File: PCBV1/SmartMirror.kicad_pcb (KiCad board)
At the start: 4 copper layers, 120 x 70 mm, 194 parts, among them J1 208658-1051, J2 502570-0893, J3 10118194-0001LF, J4 PJ-102AH, SW1 SW_DIP_x05, SW2 SW_DIP_x02, U1 MCIMX6Y2CVM08AB, U10 AP62301WU-7, U11 AP62301WU-7, U12 AP62301WU-7, U13 CP2102N-A01-GQFN28, U2 MT41K128M16JT-125_K, U3 CM1624-08DE, U4 TPD3E001DRLR, U5 MCP112T-315E_LB, U6 WF200D, U7 TFP410PAP, U8 S34ML01G200BHI000, U9 MCP112T-315E_LB, Y1 ECS-384-10-33B-CKY-TR, Y2 ECS.32712.512, Y3 ECS2401823BJTM

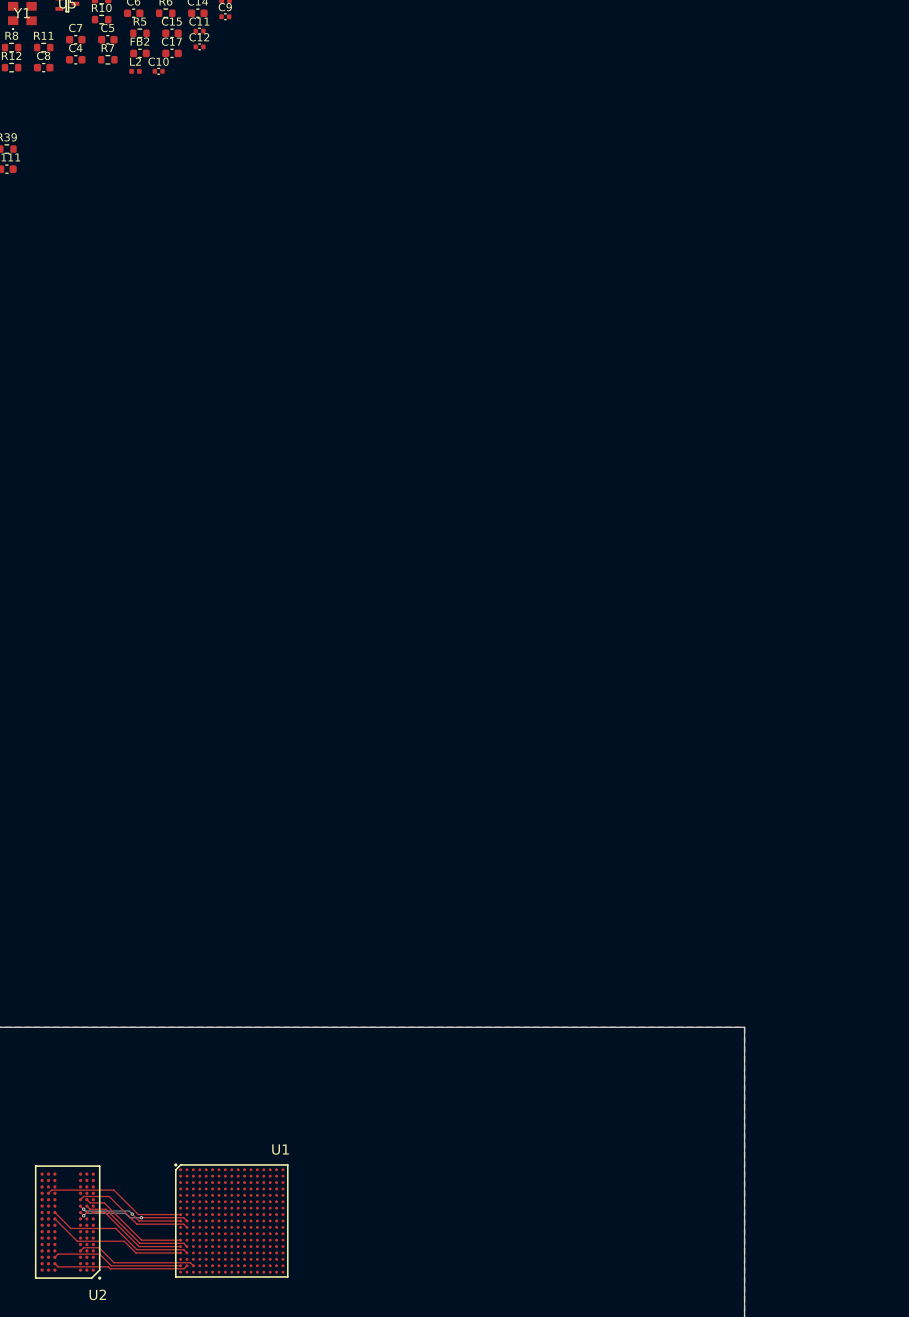
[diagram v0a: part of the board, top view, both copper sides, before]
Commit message: Added JTAG, USB OTG, USB Host, and Ethernet.
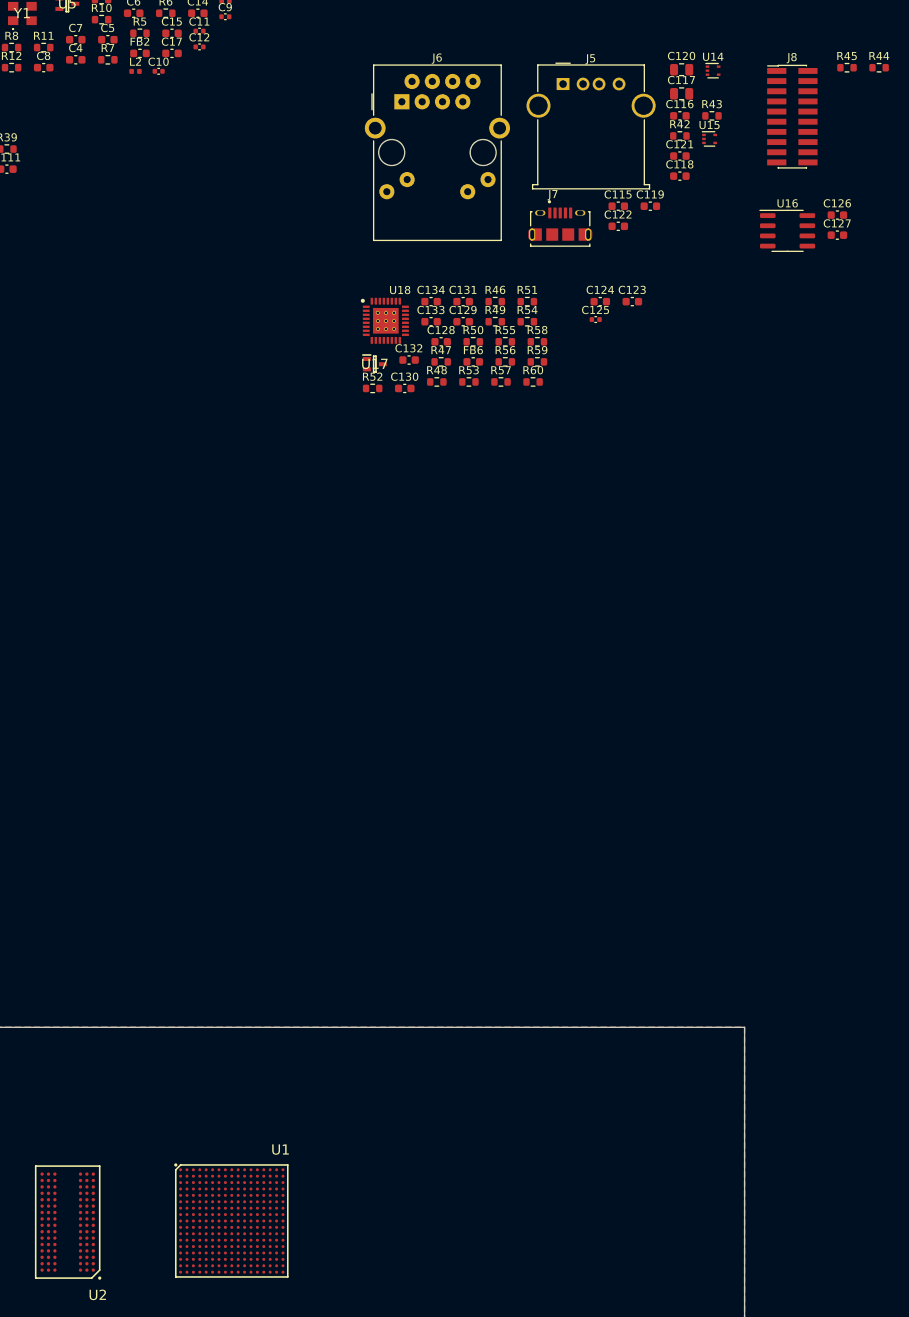
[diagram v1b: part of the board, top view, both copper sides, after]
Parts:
- added C115: 100n, Capacitor_SMD:C_0603_1608Metric, F.Cu at (199.2, -32.6)
- added C116: 100n, Capacitor_SMD:C_0603_1608Metric, F.Cu at (206.9, -43.9)
- added C117: 47u, Capacitor_SMD:C_0805_2012Metric, F.Cu at (207.1, -46.7)
- added C118: 100n, Capacitor_SMD:C_0603_1608Metric, F.Cu at (206.9, -36.4)
- added C119: 100n, Capacitor_SMD:C_0603_1608Metric, F.Cu at (203.2, -32.6)
- added C120: 47u, Capacitor_SMD:C_0805_2012Metric, F.Cu at (207.1, -49.7)
- added C121: 100n, Capacitor_SMD:C_0603_1608Metric, F.Cu at (206.9, -38.9)
- added C122: 100n, Capacitor_SMD:C_0603_1608Metric, F.Cu at (199.2, -30.1)
- added C123: 1u, Capacitor_SMD:C_0603_1608Metric, F.Cu at (201.0, -20.7)
- added C124: 1u, Capacitor_SMD:C_0603_1608Metric, F.Cu at (197.0, -20.7)
- added C125: 10u, Capacitor_SMD:C_0402_1005Metric, F.Cu at (196.4, -18.5)
- added C126: 100n, Capacitor_SMD:C_0603_1608Metric, F.Cu at (226.6, -31.5)
- added C127: 10u, Capacitor_SMD:C_0603_1608Metric, F.Cu at (226.6, -29.0)
- added C128: 100n, Capacitor_SMD:C_0603_1608Metric, F.Cu at (177.1, -15.7)
- added C129: 22u, Capacitor_SMD:C_0603_1608Metric, F.Cu at (179.8, -18.2)
- added C130: 100n, Capacitor_SMD:C_0603_1608Metric, F.Cu at (172.5, -9.86)
- added C131: 100n, Capacitor_SMD:C_0603_1608Metric, F.Cu at (179.8, -20.7)
- added C132: 22u, Capacitor_SMD:C_0603_1608Metric, F.Cu at (173.1, -13.4)
- added C133: 100n, Capacitor_SMD:C_0603_1608Metric, F.Cu at (175.8, -18.2)
- added C134: 2.2u, Capacitor_SMD:C_0603_1608Metric, F.Cu at (175.8, -20.7)
- added FB6: 600R, Inductor_SMD:L_0603_1608Metric, F.Cu at (181.1, -13.2)
- added J5: USB_A, Connector_USB:USB_A_Molex_67643_Horizontal, F.Cu at (192.3, -47.9)
- added J6: RJMG1BD3B8K1ANR, Personal_Misc:RJMG1BD3B8K1ANR, F.Cu at (172.2, -45.7)
- added J7: 10118194-0001LF, Personal_Misc:10118194-0001LF, F.Cu at (192.0, -29.1)
- added J8: Conn_02x10_Odd_Even, Connector_PinHeader_1.27mm:PinHeader_2x10_P1.27mm_Vertical_SMD, F.Cu at (221.0, -43.8)
- added R42: 220, Resistor_SMD:R_0603_1608Metric, F.Cu at (206.9, -41.4)
- added R43: 220, Resistor_SMD:R_0603_1608Metric, F.Cu at (210.9, -43.9)
- added R44: 100, Resistor_SMD:R_0603_1608Metric, F.Cu at (231.8, -49.9)
- added R45: 10k, Resistor_SMD:R_0603_1608Metric, F.Cu at (227.8, -49.9)
- added R46: 1k, Resistor_SMD:R_0603_1608Metric, F.Cu at (183.8, -20.7)
- added R47: 1k, Resistor_SMD:R_0603_1608Metric, F.Cu at (177.1, -13.2)
- added R48: 6.49k, Resistor_SMD:R_0603_1608Metric, F.Cu at (176.5, -10.7)
- added R49: 4.7k, Resistor_SMD:R_0603_1608Metric, F.Cu at (183.8, -18.2)
- added R50: 1k, Resistor_SMD:R_0603_1608Metric, F.Cu at (181.1, -15.7)
- added R51: 1k, Resistor_SMD:R_0603_1608Metric, F.Cu at (187.8, -20.7)
- added R52: 4.7k, Resistor_SMD:R_0603_1608Metric, F.Cu at (168.5, -9.86)
- added R53: 1k, Resistor_SMD:R_0603_1608Metric, F.Cu at (180.5, -10.7)
- added R54: 1k, Resistor_SMD:R_0603_1608Metric, F.Cu at (187.8, -18.2)
- added R55: 1k, Resistor_SMD:R_0603_1608Metric, F.Cu at (185.1, -15.7)
- added R56: 4.7k, Resistor_SMD:R_0603_1608Metric, F.Cu at (185.1, -13.2)
- added R57: 4.7k, Resistor_SMD:R_0603_1608Metric, F.Cu at (184.6, -10.7)
- added R58: 1k, Resistor_SMD:R_0603_1608Metric, F.Cu at (189.1, -15.7)
- added R59: 1k, Resistor_SMD:R_0603_1608Metric, F.Cu at (189.1, -13.2)
- added R60: 4.7k, Resistor_SMD:R_0603_1608Metric, F.Cu at (188.6, -10.7)
- added U14: TPD3E001DRLR, Package_TO_SOT_SMD:SOT-553, F.Cu at (211.1, -49.6)
- added U15: TPD3E001DRLR, Package_TO_SOT_SMD:SOT-553, F.Cu at (210.6, -41.0)
- added U16: MIC2026-1BM, Package_SO:SOIC-8_3.9x4.9mm_P1.27mm, F.Cu at (220.4, -29.6)
- added U17: MCP112T-315E_LB, Personal_ICs:MCP112T-315E-LB, F.Cu at (168.8, -12.9)
- added U18: KSZ8081RNB, Personal_ICs:KSZ8081RNB, F.Cu at (170.2, -18.3)
- C85: value 220n -> 100n
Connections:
- net /DDR/~DDR_CK renamed /Processor/DRAM_CLK0_N
- net /DDR/~DDR_LDQS renamed /Processor/DRAM_DQS0_N
- net /DDR/~DDR_UDQS renamed /Processor/DRAM_DQS1_N
- C3 pad 1: +5V_USB -> GND
- C3 pad 2: GND -> Net-(C3-Pad2)
- SW1 pad 6: /Video/DATA07 -> /Video/CLK
- U1 pad A8: /Video/CLK -> /Video/DATA03
- U1 pad C16: Net-(U1-PadC16) -> /Processor/ENET1_MDC
- U1 pad C17: Net-(U1-PadC17) -> /Processor/ENET1_MDIO
- U1 pad D11: /Video/DATA07 -> /Video/CLK
- U1 pad D15: Net-(U1-PadD15) -> /Processor/ENET1_RX_ER
- U1 pad D3: Net-(U1-PadD3) -> /Processor/~SD1_CD
- U1 pad E14: Net-(U1-PadE14) -> /Processor/ENET1_TX1
- U1 pad E15: Net-(U1-PadE15) -> /Processor/ENET1_TX0
- U1 pad E16: Net-(U1-PadE16) -> /Processor/ENET1_RX_EN
- U1 pad E17: Net-(U1-PadE17) -> /Processor/ENET1_RX1
- U1 pad F14: Net-(U1-PadF14) -> /Processor/ENET1_REF_CLK
- U1 pad F15: Net-(U1-PadF15) -> /Processor/ENET1_TX_EN
- U1 pad F16: Net-(U1-PadF16) -> /Processor/ENET1_RX0
- U1 pad L14: Net-(U1-PadL14) -> /Processor/USB2_PWR
- U1 pad L15: Net-(U1-PadL15) -> /Processor/USB1_OC
- U1 pad L17: /Processor/~SD1_CD -> /Processor/USB2_OC
- U1 pad M14: Net-(U1-PadM14) -> /Processor/JTAG_TCK
- U1 pad M16: Net-(U1-PadM16) -> /Processor/USB1_PWR
- U1 pad M17: Net-(U1-PadM17) -> /Processor/USB2_ID
- U1 pad N14: Net-(U1-PadN14) -> /Processor/~JTAG_TRST
- U1 pad N15: Net-(U1-PadN15) -> /Processor/JTAG_TDO
- U1 pad N16: Net-(U1-PadN16) -> /Processor/JTAG_TDI
- U1 pad P14: Net-(U1-PadP14) -> /Processor/JTAG_TMS
- U1 pad P15: Net-(U1-PadP15) -> GND
- U1 pad T12: Net-(U1-PadT12) -> +5V
- U1 pad T13: Net-(U1-PadT13) -> /Processor/USB2D_N
- U1 pad T15: Net-(U1-PadT15) -> /Processor/USB1D_N
- U1 pad U12: Net-(U1-PadU12) -> +5V
- U1 pad U13: Net-(U1-PadU13) -> /Processor/USB2D_P
- U1 pad U15: Net-(U1-PadU15) -> /Processor/USB1D_P
- U12 pad 5: Net-(U12-Pad5) -> /Power/EN
- U4 pad 1: /UART/DATA- -> /UART/DATA+
- U4 pad 2: /UART/DATA+ -> /UART/DATA-
- U7 pad 54: /Video/DATA07 -> /Video/CLK
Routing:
- net /Processor/DRAM_CLK0_N: track 18.6 -> 0.00 mm
- net /DDR/DDR_BA1: track 17.9 -> 0.00 mm
- net /DDR/DDR_CK: track 17.5 -> 0.00 mm
- net /Processor/DRAM_DQS1_N: track 16.9 -> 0.00 mm
- net /DDR/DDR_UDQS: track 16.5 -> 0.00 mm
- net /DDR/DDR_UDM: track 15.2 -> 0.00 mm
- net /DDR/DDR_BA2: track 15.1 -> 0.00 mm
- net /DDR/~DDR_CS: track 14.6 -> 0.00 mm
- net /DDR/~DDR_CAS: track 14.0 -> 0.00 mm, vias 2 -> 0
- net /DDR/DDR_BA0: track 13.8 -> 0.00 mm
- net /DDR/~DDR_WE: track 13.3 -> 0.00 mm, vias 2 -> 0
- net /DDR/DDR_ODT: track 12.7 -> 0.00 mm
- removed copper zone on In2.Cu, net GND

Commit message: Many changes to footprints (0603 -> 0402), basic DDR layout set, no traces made.
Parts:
- removed C67: 100n, Capacitor_SMD:C_0603_1608Metric
- added C135: 22u, Capacitor_SMD:C_0603_1608Metric, F.Cu at (125.9, 103.5)
- C51, C52, C53, C54, C55, C56, C57, C59, C60, C62: value 100n -> 220n; footprint Capacitor_SMD:C_0603_1608Metric -> Capacitor_SMD:C_0402_1005Metric
- C58, C61: value 100n -> 220n; footprint Capacitor_SMD:C_0603_1608Metric -> Capacitor_SMD:C_0402_1005Metric; moved to B.Cu
- C63, C65, C66: footprint Capacitor_SMD:C_0603_1608Metric -> Capacitor_SMD:C_0402_1005Metric
- R27, R29: value 1.5k -> 1.54k; footprint Resistor_SMD:R_0603_1608Metric -> Resistor_SMD:R_0402_1005Metric
- R28, R32: footprint Resistor_SMD:R_0603_1608Metric -> Resistor_SMD:R_0402_1005Metric; moved to B.Cu
- R30, R31, R36: footprint Resistor_SMD:R_0603_1608Metric -> Resistor_SMD:R_0402_1005Metric
- moved C55 147.5 mm to (137.4, 104.8), turned to 90 degrees
- moved C57 144.9 mm to (137.4, 102.9), turned to 90 degrees
- moved C52 142.6 mm to (129.2, 107.1), turned to 180 degrees
- moved C59 141.7 mm to (137.4, 101.0), turned to 90 degrees
- moved C60 140.1 mm to (127.2, 101.5), turned to 90 degrees
- moved C66 138.5 mm to (137.4, 99.1), turned to 270 degrees
- moved C54 136.5 mm to (127.2, 95.3), turned to 90 degrees
- moved C58 135.9 mm to (129.6, 98.8), turned to 270 degrees
- moved C61 135.6 mm to (135.1, 98.8), turned to 270 degrees
- moved C51 134.0 mm to (127.2, 104.1), turned to 270 degrees
- moved C64 133.3 mm to (122.8, 96.6), turned to 270 degrees
- moved R31 132.3 mm to (127.1, 98.0), turned to 90 degrees
- moved R28 131.1 mm to (131.4, 98.4), turned to 90 degrees
- moved R29 130.3 mm to (124.1, 98.2), turned to 270 degrees
- moved C62 130.2 mm to (127.2, 93.4), turned to 90 degrees
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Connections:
- net /DDR/DDR_CK renamed /DDR/DDR_CK_P
- net /DDR/DDR_LDQS renamed /DDR/DDR_LDQS_P
- net /DDR/DDR_RST renamed /Processor/DRAM_RESET
- net /DDR/DDR_UDQS renamed /DDR/DDR_UDQS_P
- net /Processor/DRAM_CLK0_N renamed /DDR/DDR_CK_N
- net /Processor/DRAM_DQS0_N renamed /DDR/DDR_LDQS_N
- net /Processor/DRAM_DQS1_N renamed /DDR/DDR_UDQS_N
- C3 pad 2: Net-(C3-Pad2) -> +5V_USB
- C63 pad 2: Net-(C63-Pad2) -> /DDR/DRAM_VREF
- C65 pad 1: Net-(C63-Pad2) -> /DDR/DRAM_VREF
- SW1 pad 6: /Video/CLK -> /Video/DATA07
- U1 pad A8: /Video/DATA03 -> /Video/CLK
- U1 pad D11: /Video/CLK -> /Video/DATA07
- U7 pad 54: /Video/CLK -> /Video/DATA07
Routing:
- net GND: track 0.00 -> 40.5 mm, vias 0 -> 66
- net +1V35: track 0.00 -> 22.3 mm, vias 0 -> 30
- net /DDR/DRAM_VREF: track 0.00 -> 11.3 mm, vias 0 -> 1
- net +3V3: track 0.00 -> 7.38 mm, vias 0 -> 13
- net Net-(C100-Pad1): track 0.00 -> 4.69 mm, vias 0 -> 4
- net /DDR/DDR_CKE: track 0.00 -> 3.76 mm, vias 0 -> 1
- net Net-(C78-Pad1): track 0.00 -> 3.33 mm, vias 0 -> 3
- net Net-(R31-Pad2): track 0.00 -> 2.99 mm
- net /Processor/DRAM_RESET: track 0.00 -> 1.65 mm, vias 0 -> 2
- net /DDR/DDR_D11: track 0.00 -> 1.12 mm, vias 0 -> 2
- net Net-(C73-Pad2): track 0.00 -> 0.60 mm, vias 0 -> 1
- net /Processor/ENET1_TX1: track 0.00 -> 0.59 mm, vias 0 -> 1
- net /Processor/~JTAG_TRST: track 0.00 -> 0.59 mm, vias 0 -> 1
- net /Processor/SD2_D0: track 0.00 -> 0.59 mm, vias 0 -> 1
- net Net-(C125-Pad1): track 0.00 -> 0.59 mm, vias 0 -> 1
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- added copper zone on In2.Cu, net +1V35
- added copper zone on In2.Cu, net +3V3

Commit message: Routing of DDR. Not finished.
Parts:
- removed C108, C68, C73, C75, C82: 220n, Capacitor_SMD:C_0402_1005Metric
- moved C58 2.96 mm to (131.2, 101.2)
- moved R27 2.96 mm to (125.7, 98.8)
- moved R29 2.96 mm to (125.7, 100.7)
- moved R30 2.96 mm to (127.7, 100.5)
- moved C135 2.96 mm to (127.5, 106.0)
- moved C51 2.96 mm to (128.8, 106.5)
- moved C53 2.96 mm to (139.0, 97.8)
- moved C54 2.96 mm to (128.8, 97.8)
- moved C56 2.96 mm to (139.0, 95.9)
- moved C57 2.96 mm to (139.0, 105.4)
- moved C59 2.96 mm to (139.0, 103.5)
- moved C60 2.96 mm to (128.8, 104.0)
- moved C61 2.96 mm to (136.8, 101.3)
- moved C62 2.96 mm to (128.8, 95.9)
- moved C63 2.96 mm to (126.7, 98.8)
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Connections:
- C100 pad 1: Net-(C100-Pad1) -> /Processor/SOC_CAP
- C101 pad 1: Net-(C100-Pad1) -> /Processor/SOC_CAP
- C102 pad 1: Net-(C100-Pad1) -> /Processor/SOC_CAP
- C78 pad 1: Net-(C78-Pad1) -> /Processor/ARM_CAP
- C79 pad 1: Net-(C78-Pad1) -> /Processor/ARM_CAP
- C80 pad 1: Net-(C78-Pad1) -> /Processor/ARM_CAP
- C99 pad 1: Net-(C100-Pad1) -> /Processor/SOC_CAP
- U1 pad G10: Net-(C78-Pad1) -> /Processor/ARM_CAP
- U1 pad G11: Net-(C78-Pad1) -> /Processor/ARM_CAP
- U1 pad G8: Net-(C82-Pad1) -> /Processor/SOC_CAP
- U1 pad G9: Net-(C78-Pad1) -> /Processor/ARM_CAP
- U1 pad H11: Net-(C73-Pad2) -> /Processor/ARM_CAP
- U1 pad H8: Net-(C75-Pad1) -> /Processor/SOC_CAP
- U1 pad J11: Net-(U1-PadJ11) -> /Processor/SOC_CAP
- U1 pad J8: Net-(C68-Pad2) -> /Processor/SOC_CAP
- U1 pad K11: Net-(U1-PadK11) -> /Processor/SOC_CAP
- U1 pad K8: Net-(C108-Pad1) -> /Processor/SOC_CAP
- U1 pad L10: Net-(C100-Pad1) -> /Processor/SOC_CAP
- U1 pad L11: Net-(C100-Pad1) -> /Processor/SOC_CAP
- U1 pad L8: Net-(C100-Pad1) -> /Processor/SOC_CAP
- U1 pad L9: Net-(C100-Pad1) -> /Processor/SOC_CAP
- U1 pad P3: /DDR/DDR_D13 -> /DDR/DDR_D12
- U1 pad P5: /DDR/DDR_D12 -> /DDR/DDR_D9
- U1 pad R1: /DDR/DDR_D15 -> /DDR/DDR_D10
- U1 pad T6: /DDR/DDR_D2 -> /DDR/DDR_D4
- U1 pad T8: /DDR/DDR_D5 -> /DDR/DDR_D1
- U1 pad U3: /DDR/DDR_D9 -> /DDR/DDR_D15
- U1 pad U4: /DDR/DDR_D7 -> /DDR/DDR_D2
- U1 pad U5: /DDR/DDR_D10 -> /DDR/DDR_D13
- U1 pad U6: /DDR/DDR_D1 -> /DDR/DDR_D7
- U1 pad U7: /DDR/DDR_D3 -> /DDR/DDR_D5
- U1 pad U8: /DDR/DDR_D4 -> /DDR/DDR_D3
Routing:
- net /DDR/DDR_D3: track 0.00 -> 32.5 mm
- net /DDR/DDR_D5: track 0.00 -> 31.7 mm
- net /DDR/DDR_D1: track 0.00 -> 31.6 mm
- net /DDR/DDR_LDQS_N: track 0.57 -> 31.3 mm, vias 1 -> 2
- net +1V35: track 22.3 -> 52.5 mm, vias 30 -> 47
- net /DDR/DDR_LDM: track 0.00 -> 29.8 mm, vias 0 -> 2
- net /DDR/DDR_D7: track 0.00 -> 29.6 mm
- net /DDR/DDR_D4: track 0.00 -> 29.3 mm
- net /DDR/DDR_LDQS_P: track 0.57 -> 29.2 mm, vias 1 -> 2
- net /DDR/DDR_D6: track 0.00 -> 28.3 mm
- net /DDR/DDR_D12: track 0.54 -> 24.9 mm, vias 1 -> 2
- net /DDR/DDR_D2: track 0.00 -> 24.0 mm
- net /DDR/DDR_CK_P: track 0.00 -> 23.4 mm, vias 0 -> 1
- net /DDR/DDR_CK_N: track 0.00 -> 23.3 mm, vias 0 -> 1
- net /DDR/DDR_D8: track 0.00 -> 22.1 mm, vias 0 -> 2
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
